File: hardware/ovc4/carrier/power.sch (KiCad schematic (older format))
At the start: 37 parts, among them J3 Conn_01x02, SW1 SW_Push, U1 Jetson_Nano, U10 TPS2121, U11 TLV70218_SOT23-5, U6 74AHC1G08, U7 TPSM53604, U8 TPS2121, U9 EN5322QI

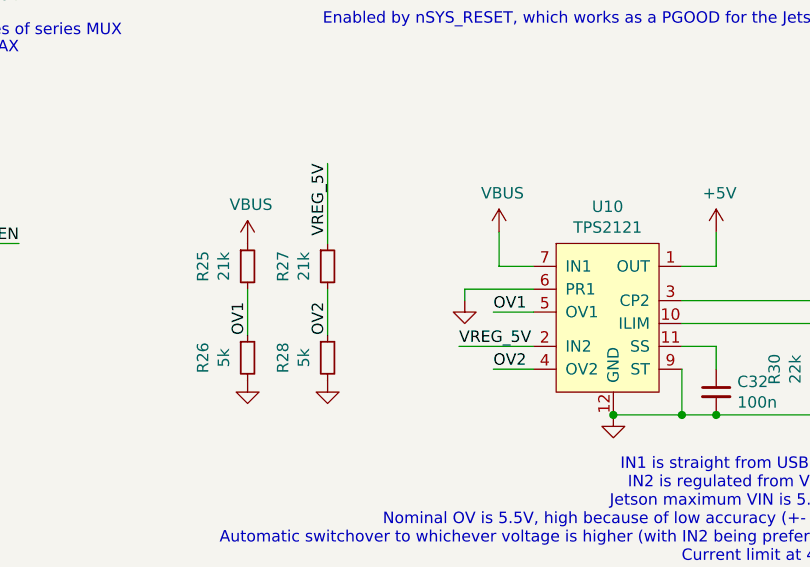
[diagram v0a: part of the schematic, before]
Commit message: Several camera interface + USB fixes
Signed-off-by: Luca Della Vedova <luca@openrobotics.org>
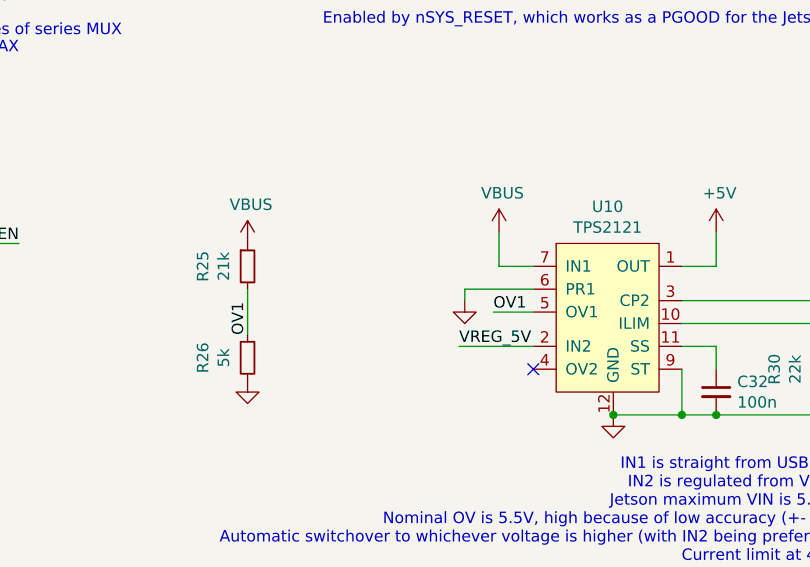
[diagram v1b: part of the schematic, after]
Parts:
- removed R27: 21k, Resistor_SMD:R_0402_1005Metric, symbol Device:R_Small
- removed R28: 5k, Resistor_SMD:R_0402_1005Metric, symbol Device:R_Small
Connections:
- net OV2: no longer names the net of U10.4 (OV2)
- no-connect marks 5 -> 6
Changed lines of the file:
@@
 NoConn ~ 6000 2250
 NoConn ~ 6000 2350
+NoConn ~ 8350 4550
 Wire Wire Line
 	625  1400 1000 1400
@@
 	7250 1950 7750 1950
 Wire Wire Line
-	7450 3650 7450 4000
-Wire Wire Line
-	7450 4200 7450 4400
-Wire Wire Line
 	7550 1300 8050 1300
 Wire Wire Line
@@
 Wire Wire Line
 	8175 4300 8350 4300
-Wire Wire Line
-	8175 4550 8350 4550
 Wire Wire Line
 	8200 4100 8200 3950
@@
 Text Label 7250 1950 0    50   ~ 0
 nSYS_RESET
-Text Label 7450 3650 3    50   ~ 0
-VREG_5V
-Text Label 7450 4400 1    50   ~ 0
-OV2
 Text Label 8025 4450 0    50   ~ 0
 VREG_5V
 Text Label 8175 4300 0    50   ~ 0
 OV1
-Text Label 8175 4550 0    50   ~ 0
-OV2
 Text Label 8900 2350 2    50   ~ 0
 V33_POK
@@
 $EndComp
 $Comp
-L power:GND #PWR0153
-U 1 1 5ECFB25E
-P 7450 4600
-F 0 "#PWR0153" H 7450 4350 50  0001 C CNN
-F 1 "GND" H 7455 4430 50  0001 C CNN
-F 2 "" H 7450 4600 50  0001 C CNN
-F 3 "" H 7450 4600 50  0001 C CNN
-	1    7450 4600
-	1    0    0    -1
-$EndComp
-$Comp
 L power:GND #PWR0160
 U 1 1 5EA75FC9
@@
 	1    0    0    -1
 $EndComp
-$Comp
-L Device:R_Small R27
-U 1 1 5ECC612B
-P 7450 4100
-F 0 "R27" V 7255 4100 50  0000 C CNN
-F 1 "21k" V 7346 4100 50  0000 C CNN
-F 2 "Resistor_SMD:R_0402_1005Metric" H 7450 4100 50  0001 C CNN
-F 3 "~" H 7450 4100 50  0001 C CNN
-	1    7450 4100
-	1    0    0    -1
-$EndComp
-$Comp
-L Device:R_Small R28
-U 1 1 5EDEB28C
-P 7450 4500
-F 0 "R28" V 7255 4500 50  0000 C CNN
-F 1 "5k" V 7346 4500 50  0000 C CNN
-F 2 "Resistor_SMD:R_0402_1005Metric" H 7450 4500 50  0001 C CNN
-F 3 "~" H 7450 4500 50  0001 C CNN
-	1    7450 4500
-	1    0    0    -1
-$EndComp
